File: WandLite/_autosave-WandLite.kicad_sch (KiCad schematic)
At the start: 17 parts, among them J4 Conn_01x03_Pin, J9 Conn_01x02_Pin, SW1 SW_SPDT_312, SW2 SW_SPDT_312, U1 ATtiny85-20P

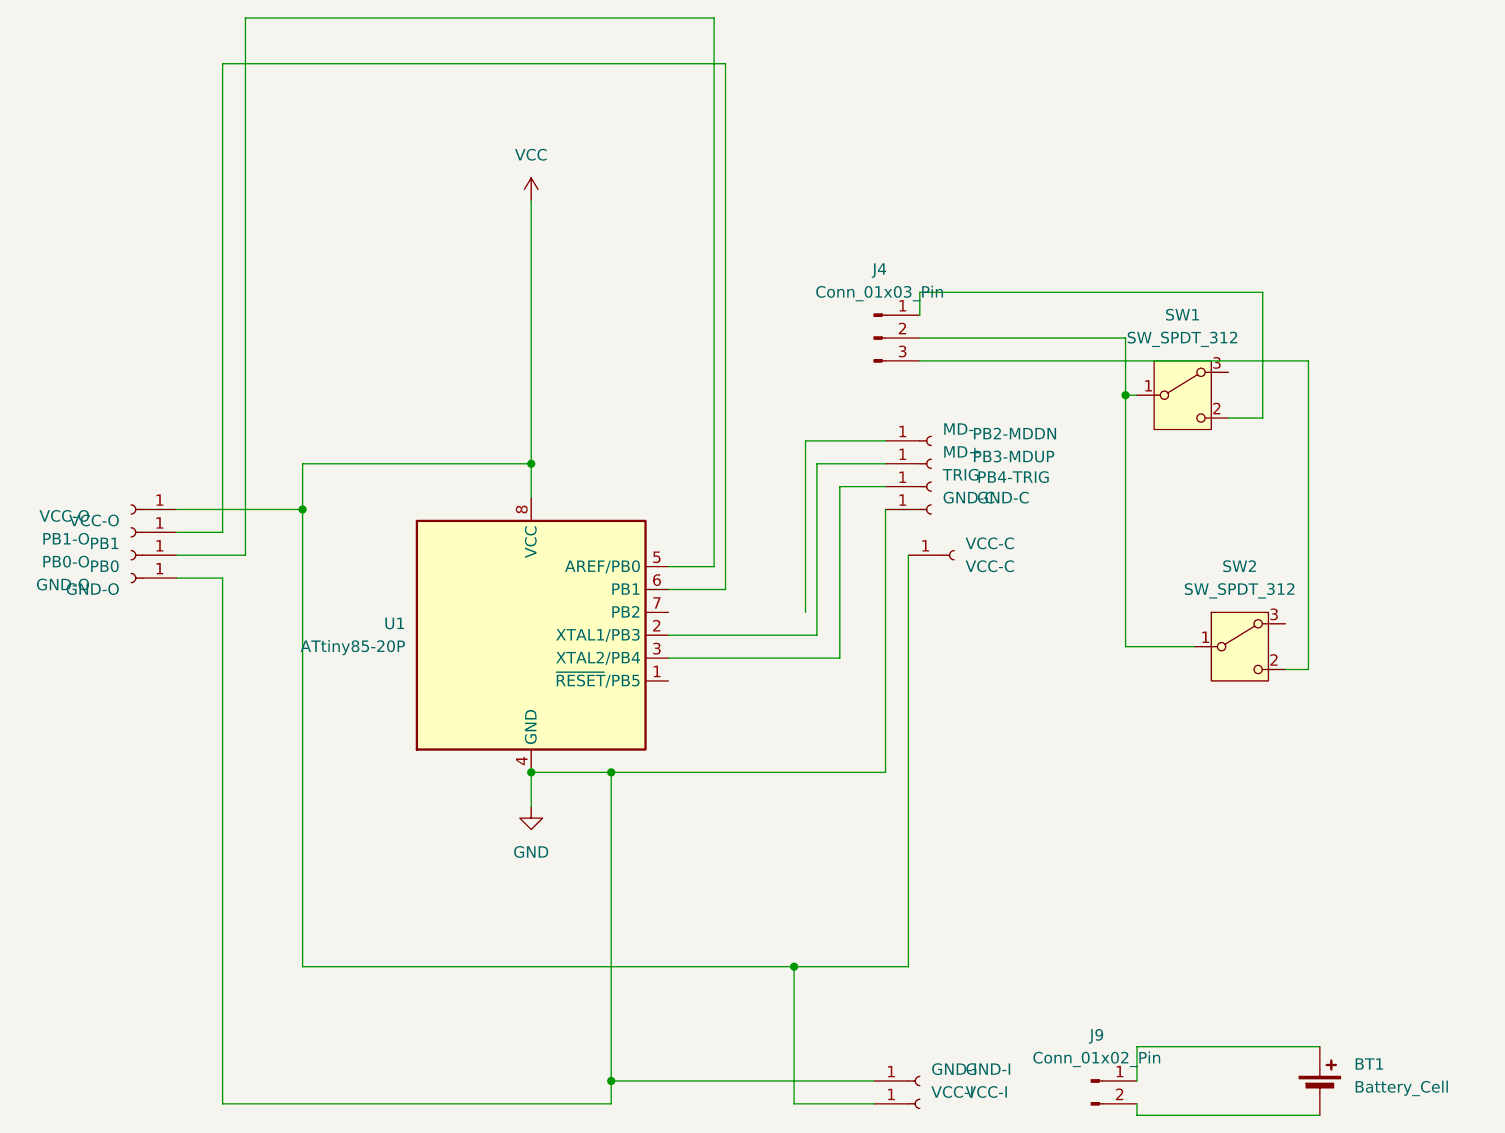
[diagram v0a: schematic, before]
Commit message: removed mode- for vcc-c
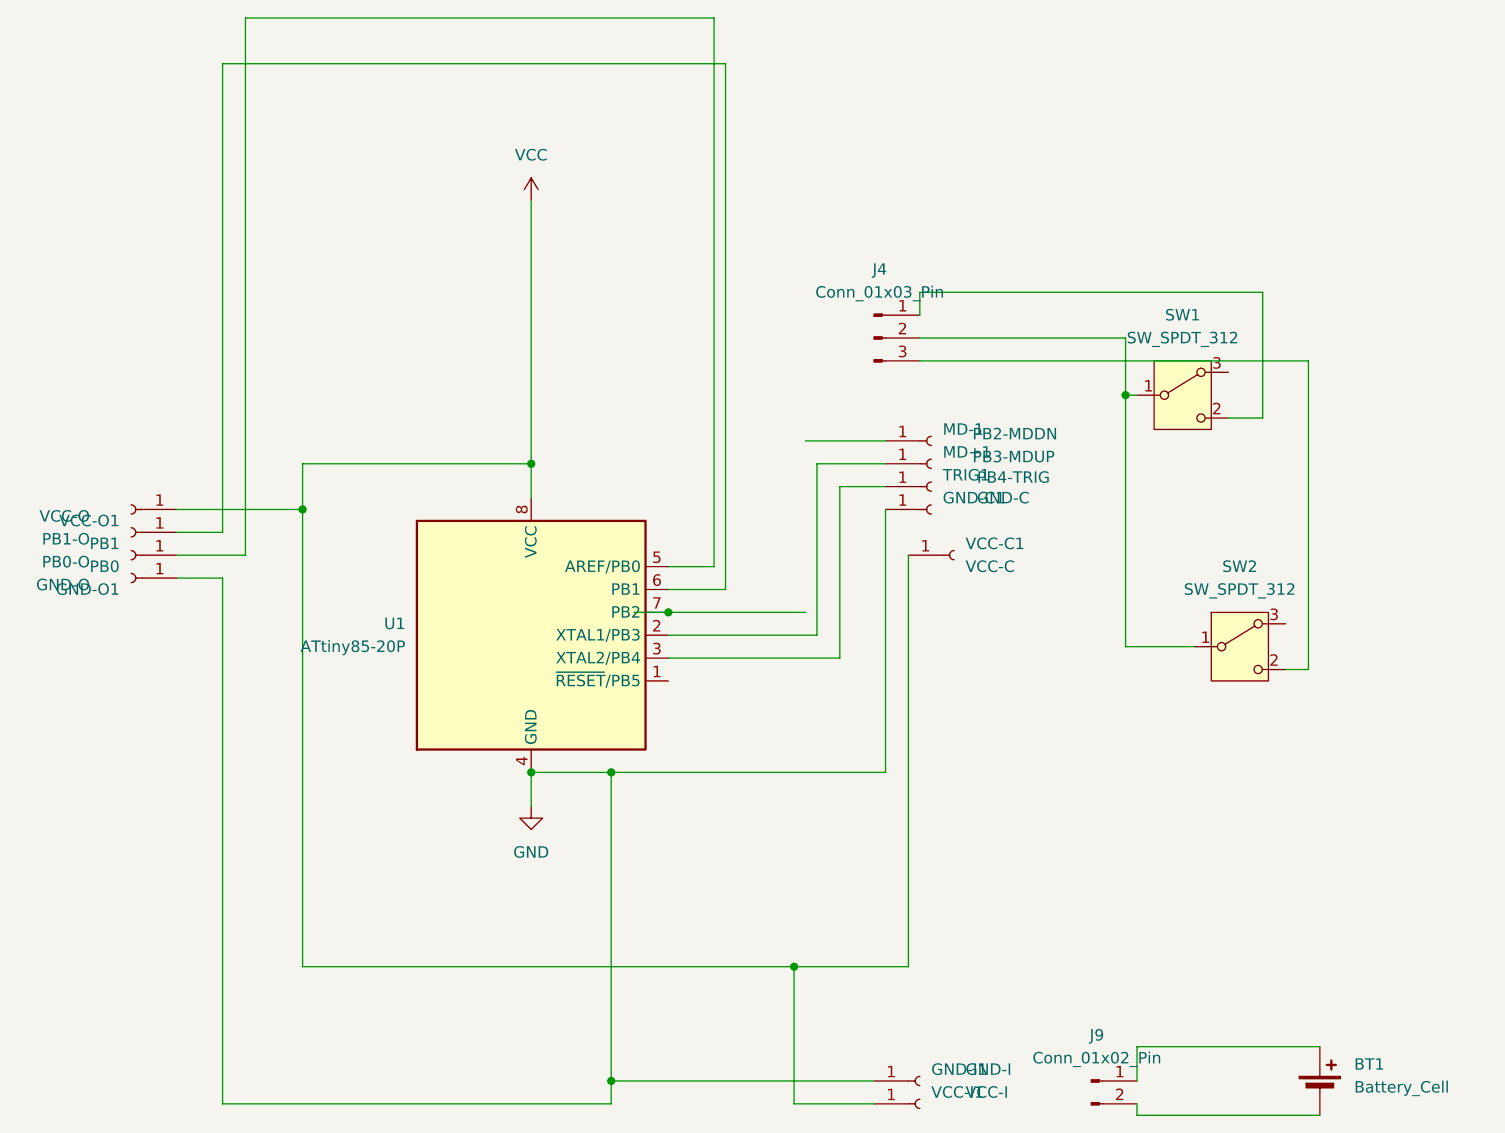
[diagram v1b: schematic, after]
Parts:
- renumbered GND-C to GND-C1, GND-I to GND-I1, GND-O to GND-O1, MD+ to MD+1, MD- to MD-1, TRIG to TRIG1, VCC-C to VCC-C1, VCC-I to VCC-I1, VCC-O to VCC-O1
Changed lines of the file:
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@@
+	)
+	(junction
+		(at 161.29 104.14)
+		(diameter 0)
+		(color 0 0 0 0)
 	)
 	(junction
@@
 	(wire
 		(pts
-			(xy 176.53 85.09) (xy 176.53 104.14)
+			(xy 157.48 104.14) (xy 161.29 104.14)
 		)
 		(stroke
@@
 		(pts
 			(xy 120.65 92.71) (xy 120.65 143.51)
+		)
+		(stroke
+			(width 0)
+			(type default)
+		)
+	)
+	(wire
+		(pts
+			(xy 161.29 104.14) (xy 176.53 104.14)
 		)
 		(stroke
@@
 		(on_board yes)
 		(dnp no)
-		(property "Reference" "MD+"
+		(property "Reference" "MD+1"
 			(at 191.77 86.3599 0)
 			(effects
@@
 			(project "WandLite"
 				(path "/ec341423-d53c-4c2b-9a9f-1b4b216b1e78"
-					(reference "MD+")
+					(reference "MD+1")
 					(unit 1)
 				)
@@
 		(on_board yes)
 		(dnp no)
-		(property "Reference" "VCC-O"
+		(property "Reference" "VCC-O1"
 			(at 100.33 93.9801 0)
 			(effects
@@
 			(project "WandLite"
 				(path "/ec341423-d53c-4c2b-9a9f-1b4b216b1e78"
-					(reference "VCC-O")
+					(reference "VCC-O1")
 					(unit 1)
 				)
@@
 		(on_board yes)
 		(dnp no)
-		(property "Reference" "GND-C"
+		(property "Reference" "GND-C1"
 			(at 191.77 91.4399 0)
 			(effects
@@
 			(project "WandLite"
 				(path "/ec341423-d53c-4c2b-9a9f-1b4b216b1e78"
-					(reference "GND-C")
+					(reference "GND-C1")
 					(unit 1)
 				)
@@
 		(on_board yes)
 		(dnp no)
-		(property "Reference" "VCC-I"
+		(property "Reference" "VCC-I1"
 			(at 190.5 157.4799 0)
 			(effects
@@
 			(project "WandLite"
 				(path "/ec341423-d53c-4c2b-9a9f-1b4b216b1e78"
-					(reference "VCC-I")
+					(reference "VCC-I1")
 					(unit 1)
 				)
@@
 		(on_board yes)
 		(dnp no)
-		(property "Reference" "GND-O"
+		(property "Reference" "GND-O1"
 			(at 100.33 101.6001 0)
 			(effects
@@
 			(project "WandLite"
 				(path "/ec341423-d53c-4c2b-9a9f-1b4b216b1e78"
-					(reference "GND-O")
+					(reference "GND-O1")
 					(unit 1)
 				)
@@
 		(dnp no)
 		(fields_autoplaced yes)
-		(property "Reference" "VCC-C"
+		(property "Reference" "VCC-C1"
 			(at 194.31 96.5199 0)
 			(effects
@@
 			(project ""
 				(path "/ec341423-d53c-4c2b-9a9f-1b4b216b1e78"
-					(reference "VCC-C")
+					(reference "VCC-C1")
 					(unit 1)
 				)
@@
 		(on_board yes)
 		(dnp no)
-		(property "Reference" "GND-I"
+		(property "Reference" "GND-I1"
 			(at 190.5 154.9399 0)
 			(effects
@@
 			(project "WandLite"
 				(path "/ec341423-d53c-4c2b-9a9f-1b4b216b1e78"
-					(reference "GND-I")
+					(reference "GND-I1")
 					(unit 1)
 				)
@@
 		(on_board yes)
 		(dnp no)
-		(property "Reference" "TRIG"
+		(property "Reference" "TRIG1"
 			(at 191.77 88.8999 0)
 			(effects
@@
 			(project "WandLite"
 				(path "/ec341423-d53c-4c2b-9a9f-1b4b216b1e78"
-					(reference "TRIG")
+					(reference "TRIG1")
 					(unit 1)
 				)
@@
 		(on_board yes)
 		(dnp no)
-		(property "Reference" "MD-"
+		(property "Reference" "MD-1"
 			(at 191.77 83.8199 0)
 			(effects
@@
 			(project ""
 				(path "/ec341423-d53c-4c2b-9a9f-1b4b216b1e78"
-					(reference "MD-")
+					(reference "MD-1")
 					(unit 1)
 				)
